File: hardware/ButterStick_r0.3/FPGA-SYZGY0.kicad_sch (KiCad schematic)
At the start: 1 part, among them U2 ECP5UM5G_85_CABGA381

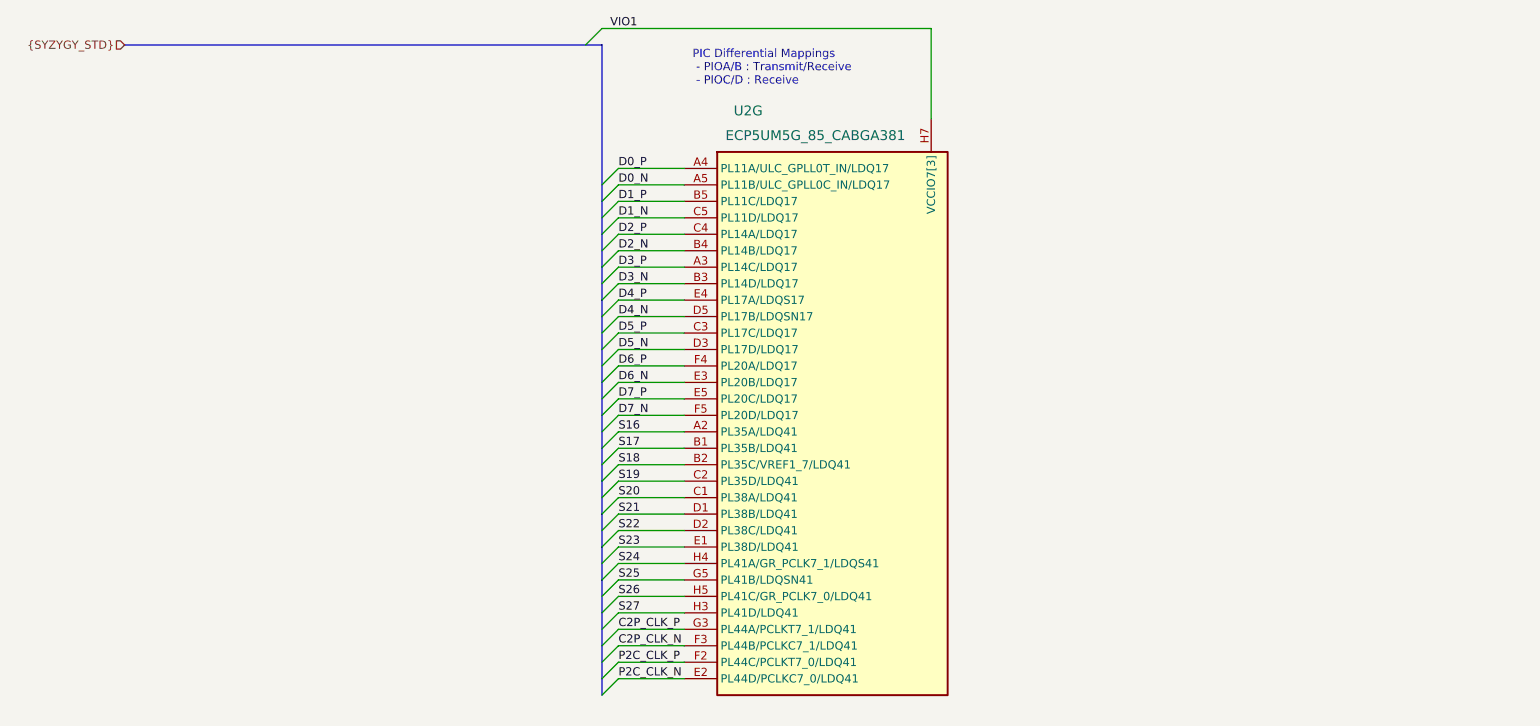
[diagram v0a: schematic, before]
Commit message: hw.r0_3: routing improvements
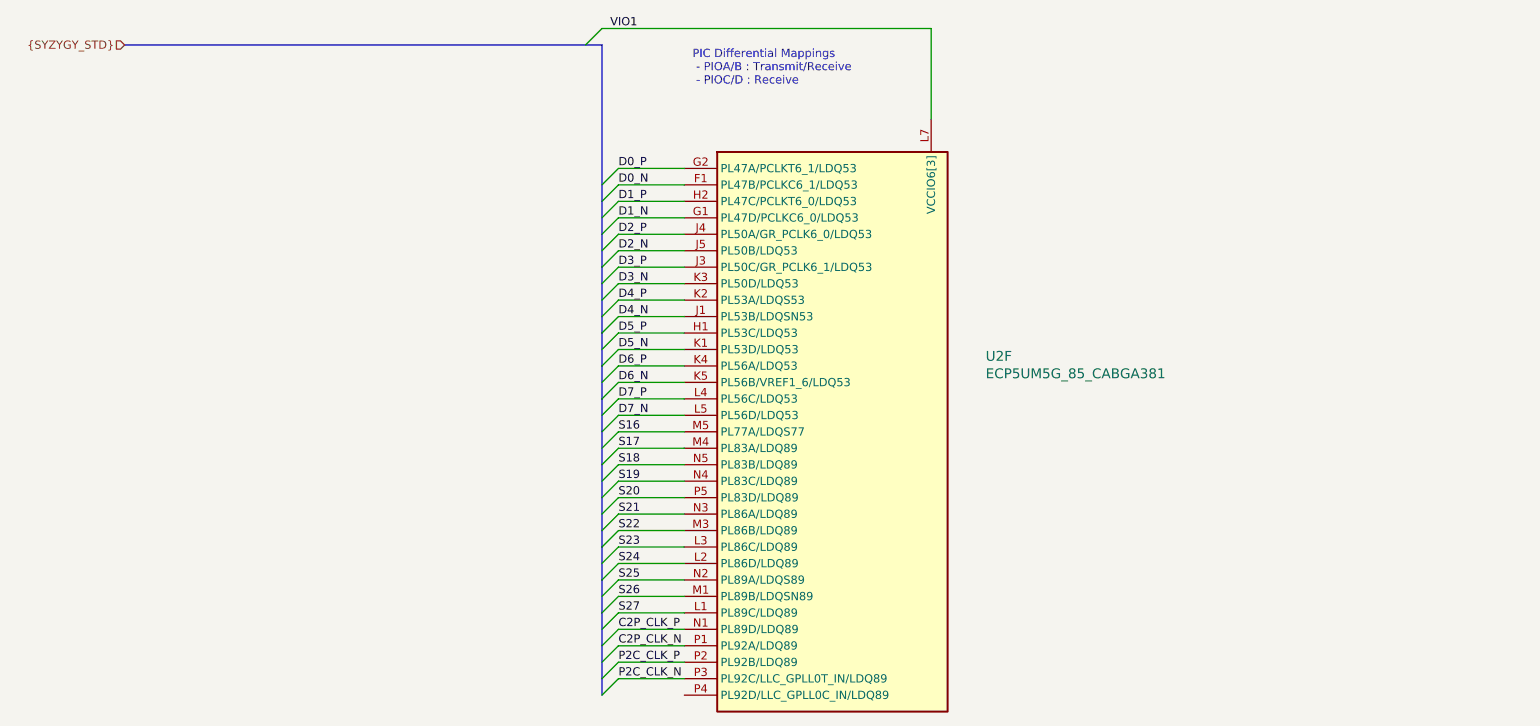
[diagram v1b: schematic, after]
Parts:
- removed U2: ECP5UM5G_85_CABGA381, gkl_housings_bga:caBGA_381_17x17, symbol gkl_lattice:ECP5UM5G_85_CABGA381
- added U2: ECP5UM5G_85_CABGA381, gkl_housings_bga:caBGA_381_17x17, symbol gkl_lattice:ECP5UM5G_85_CABGA381
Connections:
- net C2P_CLK_N: now also U2.P1 (PL92A/LDQ89)
- net C2P_CLK_P: now also U2.N1 (PL89D/LDQ89)
- net D0_N: now also U2.F1 (PL47B/PCLKC6_1/LDQ53)
- net D0_P: now also U2.G2 (PL47A/PCLKT6_1/LDQ53)
- net D1_N: now also U2.G1 (PL47D/PCLKC6_0/LDQ53)
- net D1_P: now also U2.H2 (PL47C/PCLKT6_0/LDQ53)
- net D2_N: now also U2.J5 (PL50B/LDQ53)
- net D2_P: now also U2.J4 (PL50A/GR_PCLK6_0/LDQ53)
- net D3_N: now also U2.K3 (PL50D/LDQ53)
- net D3_P: now also U2.J3 (PL50C/GR_PCLK6_1/LDQ53)
- net D4_N: now also U2.J1 (PL53B/LDQSN53)
- net D4_P: now also U2.K2 (PL53A/LDQS53)
- net D5_N: now also U2.K1 (PL53D/LDQ53)
- net D5_P: now also U2.H1 (PL53C/LDQ53)
- net D6_N: now also U2.K5 (PL56B/VREF1_6/LDQ53)
- net D6_P: now also U2.K4 (PL56A/LDQ53)
- net D7_N: now also U2.L5 (PL56D/LDQ53)
- net D7_P: now also U2.L4 (PL56C/LDQ53)
- net P2C_CLK_N: now also U2.P3 (PL92C/LLC_GPLL0T_IN/LDQ89)
- net P2C_CLK_P: now also U2.P2 (PL92B/LDQ89)
- net S16: now also U2.M5 (PL77A/LDQS77)
- net S17: now also U2.M4 (PL83A/LDQ89)
- net S18: now also U2.N5 (PL83B/LDQ89)
- net S19: now also U2.N4 (PL83C/LDQ89)
- net S20: now also U2.P5 (PL83D/LDQ89)
- net S21: now also U2.N3 (PL86A/LDQ89)
- net S22: now also U2.M3 (PL86B/LDQ89)
- net S23: now also U2.L3 (PL86C/LDQ89)
- net S24: now also U2.L2 (PL86D/LDQ89)
- net S25: now also U2.N2 (PL89A/LDQS89)
- net S26: now also U2.M1 (PL89B/LDQSN89)
- net S27: now also U2.L1 (PL89C/LDQ89)
- net VIO1: now also U2.L6 (VCCIO6[3]), U2.L7 (VCCIO6[3]), U2.M6 (VCCIO6[3])
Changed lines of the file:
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@@
 (kicad_sch (version 20200512) (host eeschema "5.99.0-unknown-c8476d6~101~ubuntu18.04.1")
-  (page 10 20)
+  (page 1 20)
   (paper "A4")
   (bus_entry (at 116.84 49.53) (size 2.54 -2.54))
@@
   (bus (pts (xy 119.38 73.66) (xy 119.38 78.74)))
   (bus (pts (xy 119.38 78.74) (xy 119.38 83.82)))
-  (bus (pts (xy 119.38 83.82) (xy 119.38 88.9)))
-  (bus (pts (xy 119.38 88.9) (xy 119.38 91.44)))
-  (bus (pts (xy 119.38 91.44) (xy 119.38 96.52)))
-  (bus (pts (xy 119.38 96.52) (xy 119.38 101.6)))
-  (bus (pts (xy 119.38 101.6) (xy 119.38 106.68)))
-  (bus (pts (xy 119.38 106.68) (xy 119.38 111.76)))
-  (bus (pts (xy 119.38 111.76) (xy 119.38 116.84)))
-  (bus (pts (xy 119.38 116.84) (xy 119.38 121.92)))
-  (bus (pts (xy 119.38 121.92) (xy 119.38 127)))
+  (bus (pts (xy 119.38 83.82) (xy 119.38 86.36)))
+  (bus (pts (xy 119.38 86.36) (xy 119.38 91.44)))
+  (bus (pts (xy 119.38 91.44) (xy 119.38 93.98)))
+  (bus (pts (xy 119.38 93.98) (xy 119.38 99.06)))
+  (bus (pts (xy 119.38 99.06) (xy 119.38 104.14)))
+  (bus (pts (xy 119.38 104.14) (xy 119.38 109.22)))
+  (bus (pts (xy 119.38 109.22) (xy 119.38 114.3)))
+  (bus (pts (xy 119.38 114.3) (xy 119.38 119.38)))
+  (bus (pts (xy 119.38 119.38) (xy 119.38 124.46)))
+  (bus (pts (xy 119.38 124.46) (xy 119.38 127)))
   (bus (pts (xy 119.38 127) (xy 119.38 132.08)))
   (bus (pts (xy 119.38 132.08) (xy 119.38 137.16)))
@@
     (effects (font (size 1.27 1.27)) (justify right))
   )
-  (symbol (lib_id "gkl_lattice:ECP5UM5G_85_CABGA381") (at 132.08 68.58 0) (unit 7)
-    (property "Reference" "U2" (id 0) (at 139.7 59.69 0)
+  (symbol (lib_id "gkl_lattice:ECP5UM5G_85_CABGA381") (at 132.08 68.58 0) (unit 6)
+    (property "Reference" "U2" (id 0) (at 178.5874 97.5614 0)
       (effects (font (size 1.524 1.524)) (justify left))
     )
-    (property "Value" "ECP5UM5G_85_CABGA381" (id 1) (at 138.43 63.5 0)
+    (property "Value" "ECP5UM5G_85_CABGA381" (id 1) (at 178.5874 100.2538 0)
       (effects (font (size 1.524 1.524)) (justify left))
     )

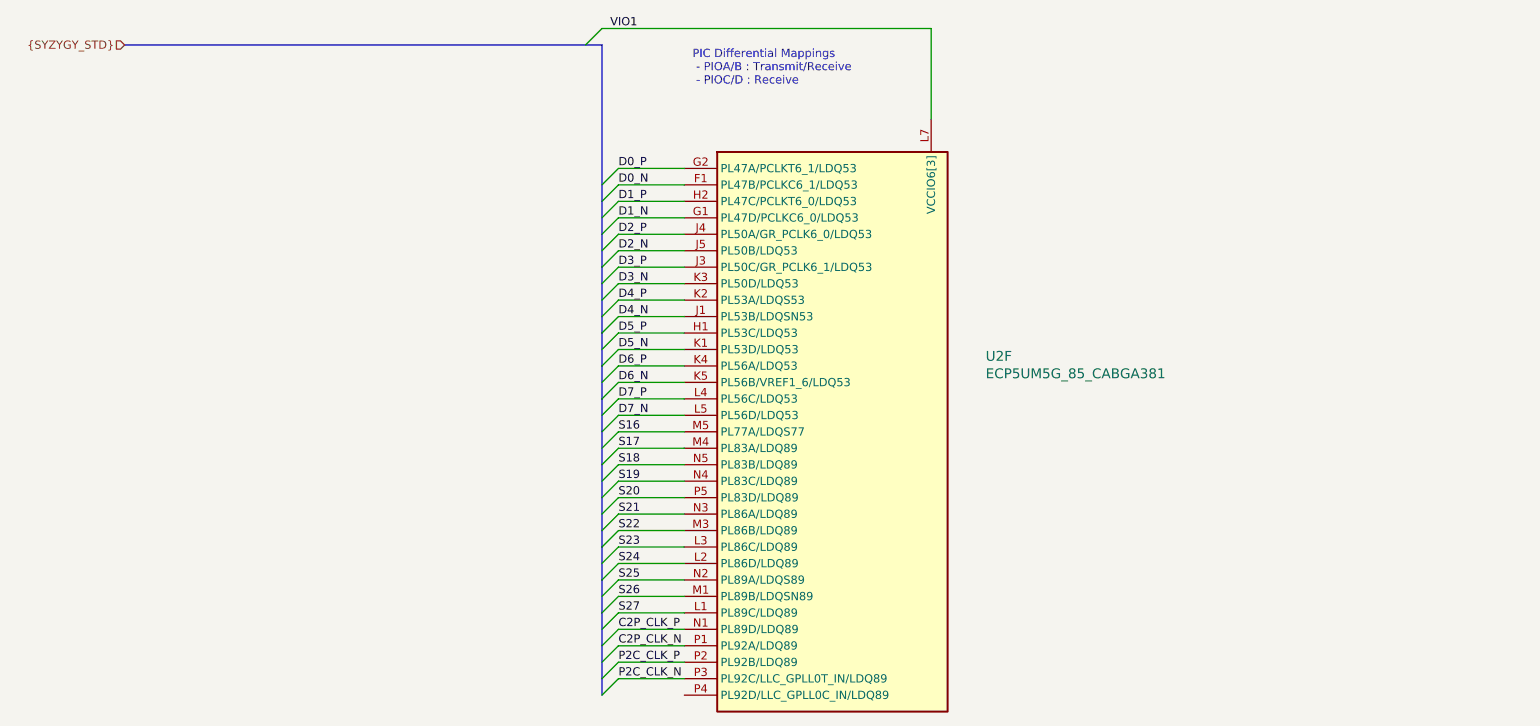
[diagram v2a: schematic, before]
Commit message: hw.r0_3: routed SYZYGY, begin routing RGMII/ULPI
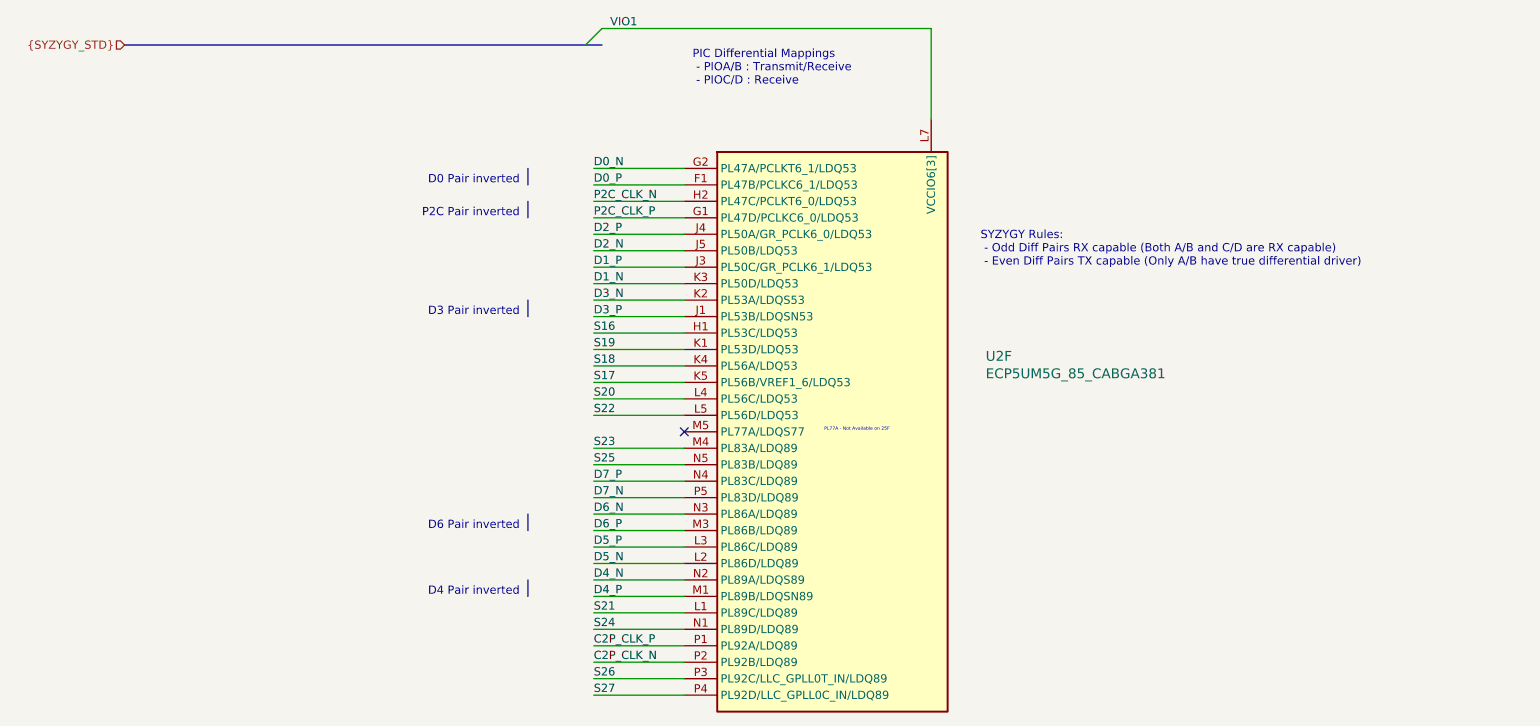
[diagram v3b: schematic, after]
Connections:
- net C2P_CLK_N: now also U2.P2 (PL92B/LDQ89); no longer U2.P1 (PL92A/LDQ89)
- net C2P_CLK_P: now also U2.P1 (PL92A/LDQ89); no longer U2.N1 (PL89D/LDQ89)
- net D0_N: now also U2.G2 (PL47A/PCLKT6_1/LDQ53); no longer U2.F1 (PL47B/PCLKC6_1/LDQ53)
- net D0_P: now also U2.F1 (PL47B/PCLKC6_1/LDQ53); no longer U2.G2 (PL47A/PCLKT6_1/LDQ53)
- net D1_N: now also U2.K3 (PL50D/LDQ53); no longer U2.G1 (PL47D/PCLKC6_0/LDQ53)
- net D1_P: now also U2.J3 (PL50C/GR_PCLK6_1/LDQ53); no longer U2.H2 (PL47C/PCLKT6_0/LDQ53)
- net D3_N: now also U2.K2 (PL53A/LDQS53); no longer U2.K3 (PL50D/LDQ53)
- net D3_P: now also U2.J1 (PL53B/LDQSN53); no longer U2.J3 (PL50C/GR_PCLK6_1/LDQ53)
- net D4_N: now also U2.N2 (PL89A/LDQS89); no longer U2.J1 (PL53B/LDQSN53)
- net D4_P: now also U2.M1 (PL89B/LDQSN89); no longer U2.K2 (PL53A/LDQS53)
- net D5_N: now also U2.L2 (PL86D/LDQ89); no longer U2.K1 (PL53D/LDQ53)
- net D5_P: now also U2.L3 (PL86C/LDQ89); no longer U2.H1 (PL53C/LDQ53)
- net D6_N: now also U2.N3 (PL86A/LDQ89); no longer U2.K5 (PL56B/VREF1_6/LDQ53)
- net D6_P: now also U2.M3 (PL86B/LDQ89); no longer U2.K4 (PL56A/LDQ53)
- net D7_N: now also U2.P5 (PL83D/LDQ89); no longer U2.L5 (PL56D/LDQ53)
- net D7_P: now also U2.N4 (PL83C/LDQ89); no longer U2.L4 (PL56C/LDQ53)
- net P2C_CLK_N: now also U2.H2 (PL47C/PCLKT6_0/LDQ53); no longer U2.P3 (PL92C/LLC_GPLL0T_IN/LDQ89)
- net P2C_CLK_P: now also U2.G1 (PL47D/PCLKC6_0/LDQ53); no longer U2.P2 (PL92B/LDQ89)
- net S16: now also U2.H1 (PL53C/LDQ53); no longer U2.M5 (PL77A/LDQS77)
- net S17: now also U2.K5 (PL56B/VREF1_6/LDQ53); no longer U2.M4 (PL83A/LDQ89)
- net S18: now also U2.K4 (PL56A/LDQ53); no longer U2.N5 (PL83B/LDQ89)
- net S19: now also U2.K1 (PL53D/LDQ53); no longer U2.N4 (PL83C/LDQ89)
- net S20: now also U2.L4 (PL56C/LDQ53); no longer U2.P5 (PL83D/LDQ89)
- net S21: now also U2.L1 (PL89C/LDQ89); no longer U2.N3 (PL86A/LDQ89)
- net S22: now also U2.L5 (PL56D/LDQ53); no longer U2.M3 (PL86B/LDQ89)
- net S23: now also U2.M4 (PL83A/LDQ89); no longer U2.L3 (PL86C/LDQ89)
- net S24: now also U2.N1 (PL89D/LDQ89); no longer U2.L2 (PL86D/LDQ89)
- net S25: now also U2.N5 (PL83B/LDQ89); no longer U2.N2 (PL89A/LDQS89)
- net S26: now also U2.P3 (PL92C/LLC_GPLL0T_IN/LDQ89); no longer U2.M1 (PL89B/LDQSN89)
- net S27: now also U2.P4 (PL92D/LLC_GPLL0C_IN/LDQ89); no longer U2.L1 (PL89C/LDQ89)
- no-connect marks 0 -> 1
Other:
- note added: "D0 Pair inverted"
- note added: "D3 Pair inverted"
- note added: "D4 Pair inverted"
- note added: "D6 Pair inverted"
- note added: "P2C Pair inverted"
- note added: "PL77A - Not Available on 25F"
- note added: "SYZYGY Rules: - Odd Diff Pairs RX capable (Both A/B and C/D are RX capable) - Even Diff Pairs TX capable (Only A/B have true differential driver)"

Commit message: hw.r0_3: major blocks roughly routed
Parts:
- renumbered U2 to U4
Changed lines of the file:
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@@
   )
   (symbol (lib_id "gkl_lattice:ECP5UM5G_85_CABGA381") (at 132.08 68.58 0) (unit 6)
-    (property "Reference" "U2" (id 0) (at 178.5874 97.5614 0)
+    (property "Reference" "U4" (id 0) (at 178.5874 97.5614 0)
       (effects (font (size 1.524 1.524)) (justify left))
     )
